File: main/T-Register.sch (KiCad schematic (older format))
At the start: 19 parts, among them U13 74LS245, U14 74LS173, U15 74LS173

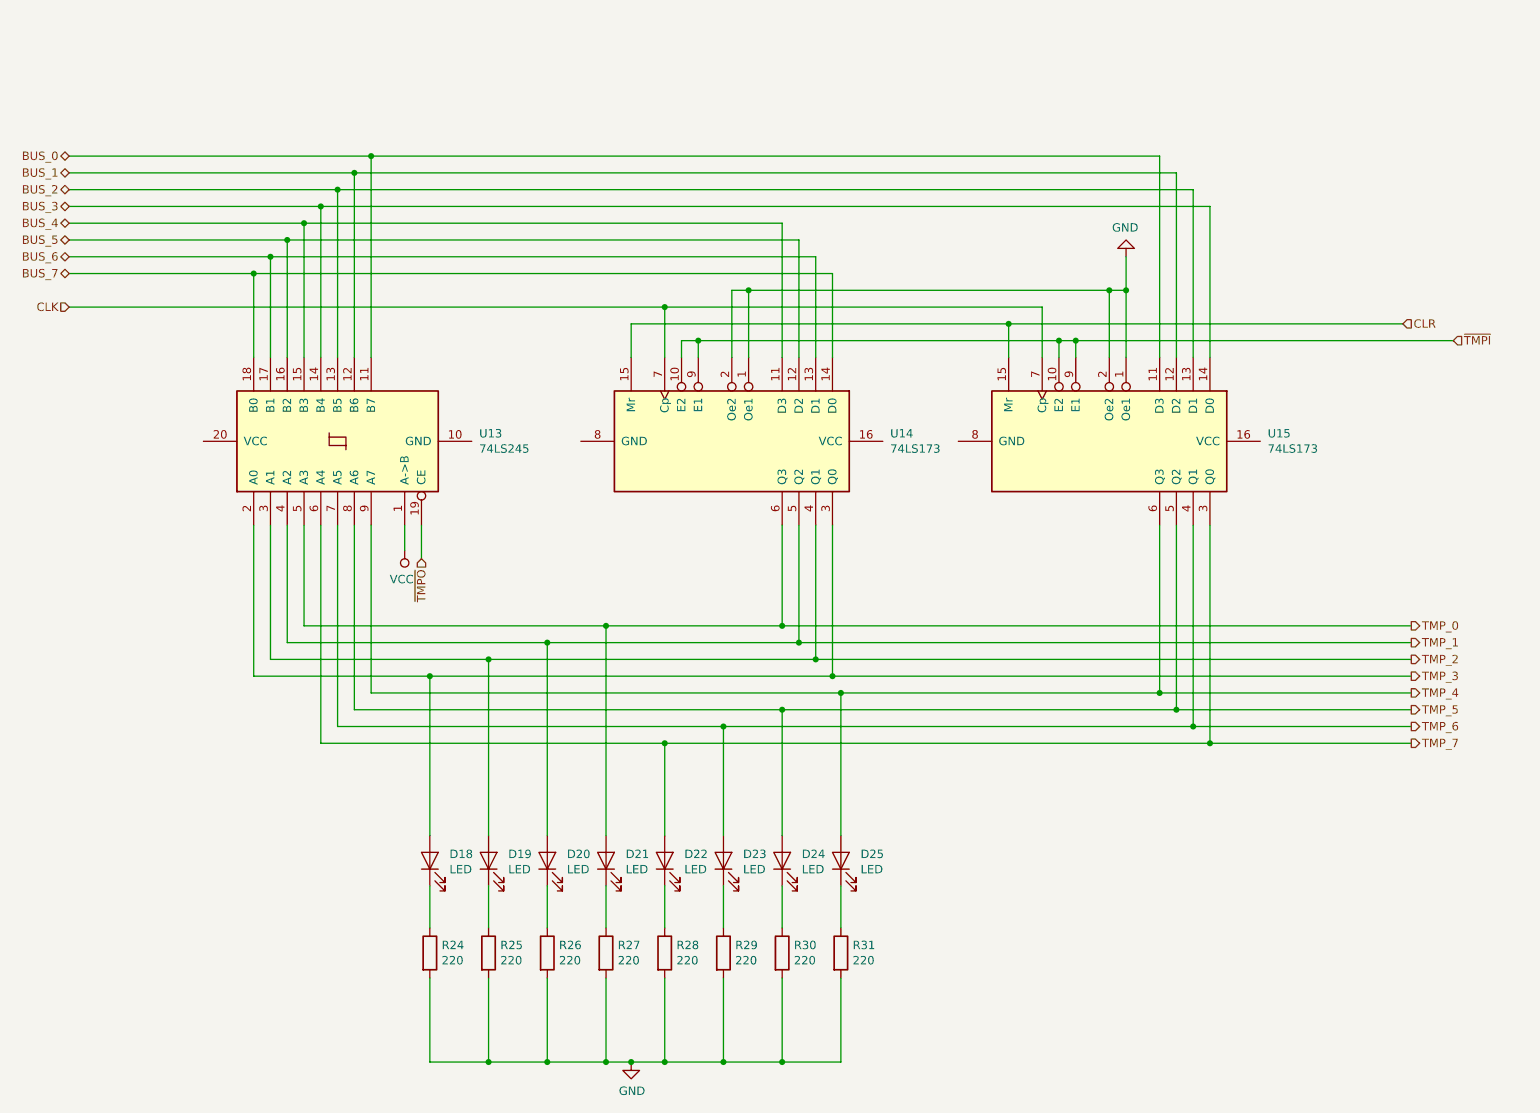
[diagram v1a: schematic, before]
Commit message: Switch to using 74LS377 in place of two 74LS173
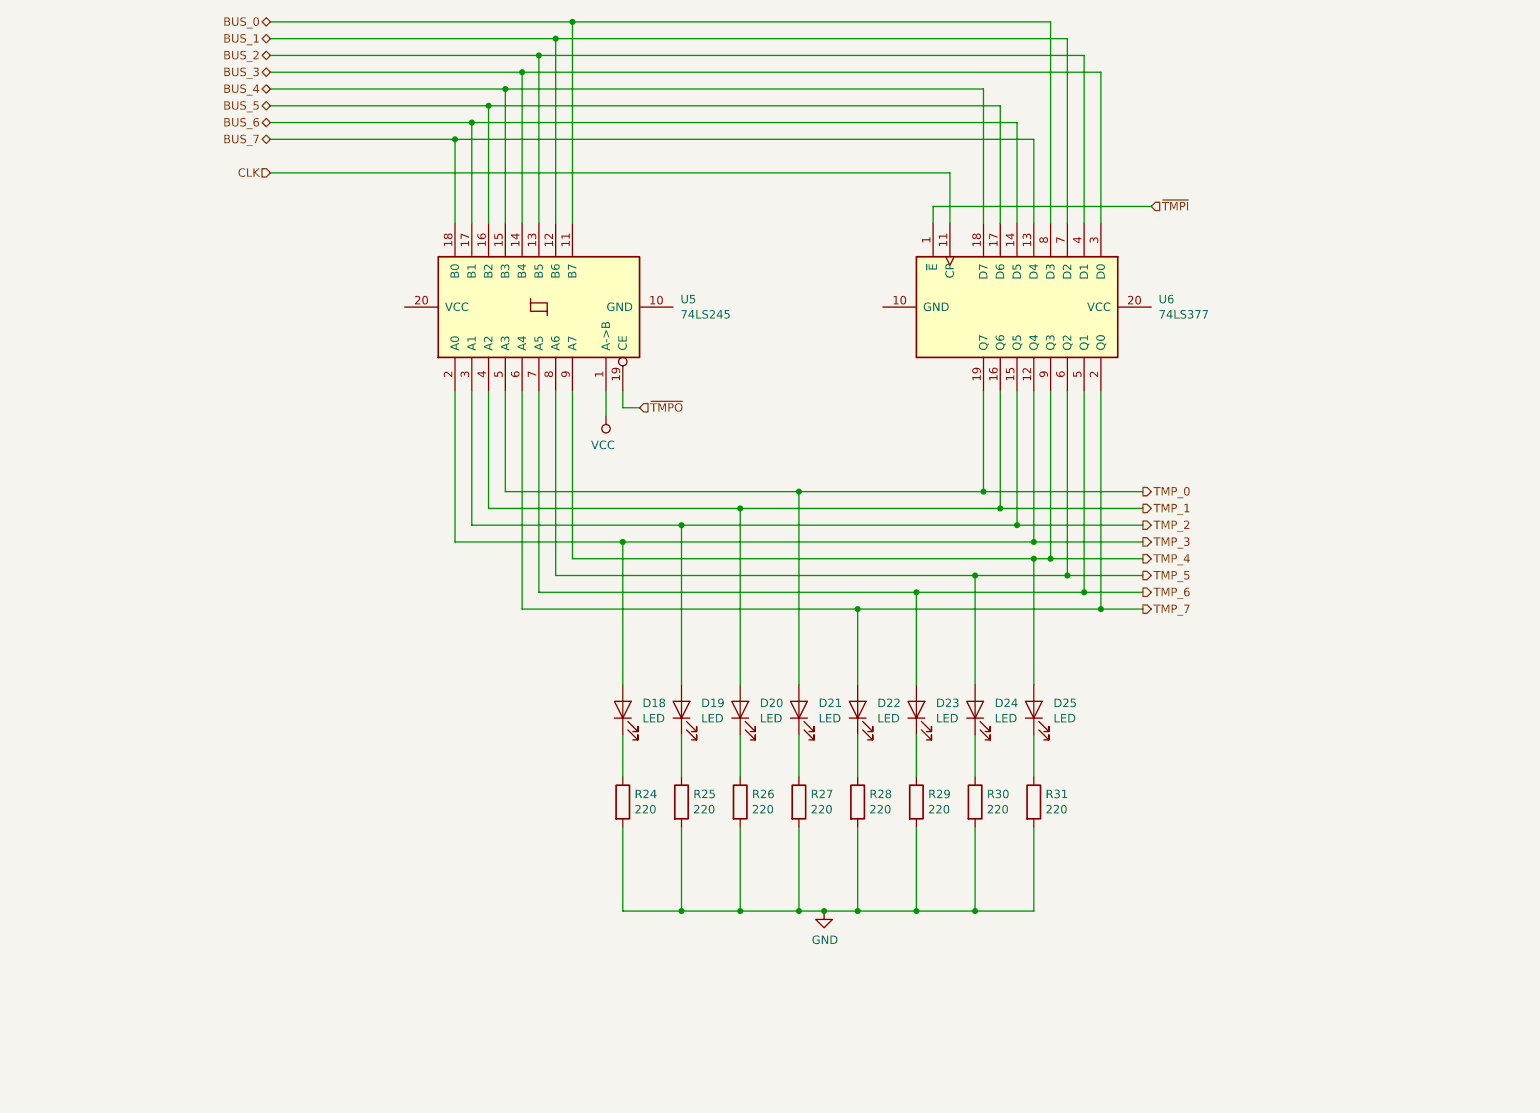
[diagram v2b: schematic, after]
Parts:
- removed U13: 74LS245, symbol 74xx:74LS245
- removed U14, U15: 74LS173, symbol 74xx:74LS173
- added U5: 74LS245, symbol 74xx:74LS245
- added U6: 74LS377, symbol 74xx:74LS377
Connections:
- net BUS_0: now also U5.11 (B7), U6.8 (D3)
- net BUS_1: now also U5.12 (B6), U6.7 (D2)
- net BUS_2: now also U5.13 (B5), U6.4 (D1)
- net BUS_3: now also U5.14 (B4), U6.3 (D0)
- net BUS_4: now also U5.15 (B3), U6.18 (D7)
- net BUS_5: now also U5.16 (B2), U6.17 (D6)
- net BUS_6: now also U5.17 (B1), U6.14 (D5)
- net BUS_7: now also U5.18 (B0), U6.13 (D4)
- net CLK: now also U6.11 (CP)
- net TMP_0: now also U5.5 (A3), U6.19 (Q7)
- net TMP_1: now also U5.4 (A2), U6.16 (Q6)
- net TMP_2: now also U5.3 (A1), U6.15 (Q5)
- net TMP_3: now also U5.2 (A0), U6.12 (Q4)
- net TMP_4: now also U5.9 (A7), U6.9 (Q3)
- net TMP_5: now also U5.8 (A6), U6.6 (Q2)
- net TMP_6: now also U5.7 (A5), U6.5 (Q1)
- net TMP_7: now also U5.6 (A4), U6.2 (Q0)
- net VCC: now also U5.1 (A->B)
- net ~TMPI~: now also U6.1 (~E)
- net ~TMPO~: now also U5.19 (CE)
